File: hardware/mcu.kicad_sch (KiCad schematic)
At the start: 16 parts, among them U1 STM32G0C1KCTxN

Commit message: new pcb layout & can coppied from steeringwheel
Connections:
- net USB.+: no longer names the net of U1.23 (PA12/PA10)
- net USB.-: no longer names the net of U1.22 (PA11/PA9)
- no-connect marks 3 -> 5
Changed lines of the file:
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@@
 	)
 	(no_connect
+		(at 179.07 114.3)
+	)
+	(no_connect
 		(at 140.97 121.92)
 	)
@@
 	)
 	(no_connect
+		(at 179.07 116.84)
+	)
+	(no_connect
 		(at 140.97 124.46)
 	)
@@
 	)
 	(bus_entry
-		(at 194.31 114.3)
-		(size 2.54 -2.54)
-		(stroke
-			(width 0)
-			(type default)
-		)
-	)
-	(bus_entry
 		(at 194.31 93.98)
 		(size 2.54 -2.54)
@@
 	)
 	(bus_entry
-		(at 196.85 114.3)
-		(size -2.54 2.54)
-		(stroke
-			(width 0)
-			(type default)
-		)
-	)
-	(bus_entry
 		(at 194.31 91.44)
 		(size 2.54 -2.54)
@@
 		)
 	)
-	(bus_entry
-		(at 196.85 111.76)
-		(size -2.54 2.54)
-		(stroke
-			(width 0)
-			(type default)
-		)
-	)
 	(wire
 		(pts
@@
 	(bus
 		(pts
-			(xy 196.85 109.22) (xy 200.66 109.22)
-		)
-		(stroke
-			(width 0)
-			(type default)
-		)
-	)
-	(bus
-		(pts
 			(xy 196.85 86.36) (xy 196.85 83.82)
 		)
@@
 	(wire
 		(pts
-			(xy 194.31 116.84) (xy 179.07 116.84)
-		)
-		(stroke
-			(width 0)
-			(type default)
-		)
-	)
-	(wire
-		(pts
 			(xy 101.6 64.77) (xy 101.6 68.58)
 		)
@@
 	(bus
 		(pts
-			(xy 196.85 111.76) (xy 196.85 114.3)
-		)
-		(stroke
-			(width 0)
-			(type default)
-		)
-	)
-	(bus
-		(pts
 			(xy 123.19 121.92) (xy 123.19 119.38)
 		)
@@
 		)
 	)
-	(wire
-		(pts
-			(xy 179.07 114.3) (xy 194.31 114.3)
-		)
-		(stroke
-			(width 0)
-			(type default)
-		)
-	)
 	(bus
 		(pts
@@
 		)
 	)
-	(bus
-		(pts
-			(xy 196.85 109.22) (xy 196.85 111.76)
-		)
-		(stroke
-			(width 0)
-			(type default)
-		)
-	)
 	(wire
 		(pts
@@
 		)
 	)
-	(label "USB.-"
-		(at 194.31 114.3 180)
-		(effects
-			(font
-				(size 1.27 1.27)
-			)
-			(justify right bottom)
-		)
-	)
 	(label "FUSE_IS3"
 		(at 194.31 93.98 180)
@@
 		)
 	)
-	(label "USB.+"
-		(at 194.31 116.84 180)
-		(effects
-			(font
-				(size 1.27 1.27)
-			)
-			(justify right bottom)
-		)
-	)
 	(label "SPI.SCK"
 		(at 194.31 99.06 180)
@@
 		)
 	)
-	(hierarchical_label "USB{- +}"
-		(shape bidirectional)
-		(at 200.66 109.22 0)
-		(effects
-			(font
-				(size 1.27 1.27)
-			)
-			(justify left)
-		)
-	)
 	(hierarchical_label "CAN{RX TX}"
 		(shape bidirectional)
@@
 		)
 		(instances
-			(project ""
+			(project "PUTM_EV_PDMv2_2024"
 				(path "/b652b05a-4e3d-4ad1-b032-18886abe7d45/44511ce6-951c-4505-8af7-9d44a269eea4"
 					(reference "D4")
@@
 		)
 		(instances
-			(project ""
+			(project "PUTM_EV_PDMv2_2024"
 				(path "/b652b05a-4e3d-4ad1-b032-18886abe7d45/44511ce6-951c-4505-8af7-9d44a269eea4"
 					(reference "#FLG01")
@@
 		)
 		(instances
-			(project ""
+			(project "PUTM_EV_PDMv2_2024"
 				(path "/b652b05a-4e3d-4ad1-b032-18886abe7d45/44511ce6-951c-4505-8af7-9d44a269eea4"
 					(reference "R4")
@@
 		)
 		(instances
-			(project ""
+			(project "PUTM_EV_PDMv2_2024"
 				(path "/b652b05a-4e3d-4ad1-b032-18886abe7d45/44511ce6-951c-4505-8af7-9d44a269eea4"
 					(reference "#PWR01")

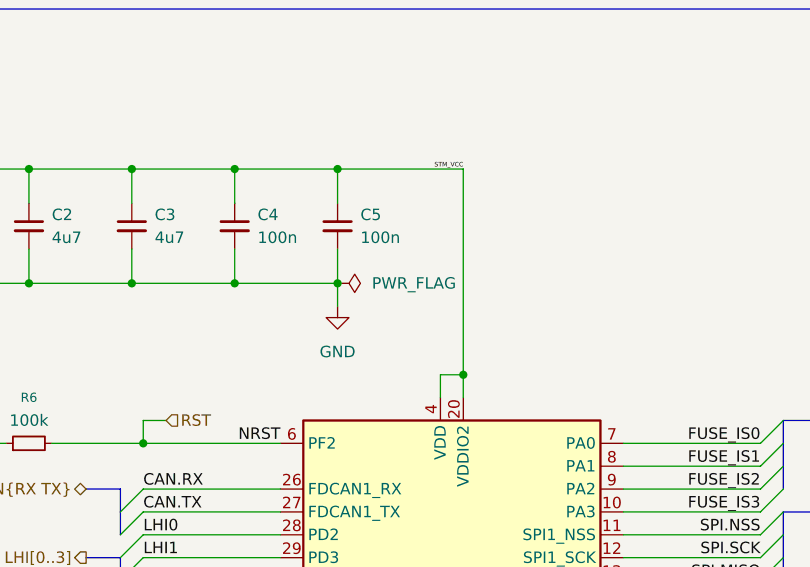
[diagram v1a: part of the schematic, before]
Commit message: pcb layout-power section 5V update
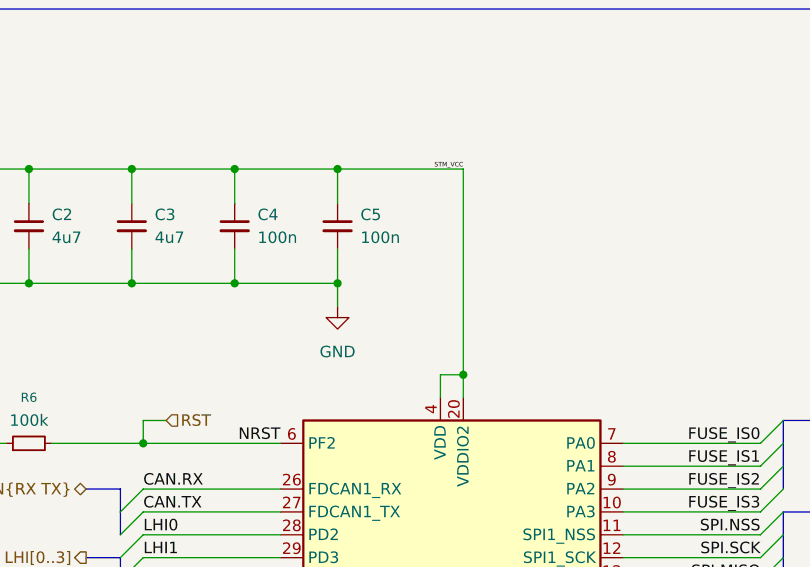
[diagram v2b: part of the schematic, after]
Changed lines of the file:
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@@
-	)
-	(symbol
-		(lib_id "power:PWR_FLAG")
-		(at 147.32 68.58 270)
-		(unit 1)
-		(exclude_from_sim no)
-		(in_bom yes)
-		(on_board yes)
-		(dnp no)
-		(fields_autoplaced yes)
-		(property "Reference" "#FLG02"
-			(at 149.225 68.58 0)
-			(effects
-				(font
-					(size 1.27 1.27)
-				)
-				(hide yes)
-			)
-		)
-		(property "Value" "PWR_FLAG"
-			(at 151.13 68.5799 90)
-			(effects
-				(font
-					(size 1.27 1.27)
-				)
-				(justify left)
-			)
-		)
-		(property "Footprint" ""
-			(at 147.32 68.58 0)
-			(effects
-				(font
-					(size 1.27 1.27)
-				)
-				(hide yes)
-			)
-		)
-		(property "Datasheet" "~"
-			(at 147.32 68.58 0)
-			(effects
-				(font
-					(size 1.27 1.27)
-				)
-				(hide yes)
-			)
-		)
-		(property "Description" "Special symbol for telling ERC where power comes from"
-			(at 147.32 68.58 0)
-			(effects
-				(font
-					(size 1.27 1.27)
-				)
-				(hide yes)
-			)
-		)
-		(pin "1"
-		)
-		(instances
-			(project "PUTM_EV_PDMv2_2024"
-				(path "/b652b05a-4e3d-4ad1-b032-18886abe7d45/44511ce6-951c-4505-8af7-9d44a269eea4"
-					(reference "#FLG02")
-					(unit 1)
-				)
-			)
-		)
 	)
 	(symbol
